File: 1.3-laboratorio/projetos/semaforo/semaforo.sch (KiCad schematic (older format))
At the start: 40 parts, among them U1 4093, U2 4093, U3 12V, U4 4017, U5 4017

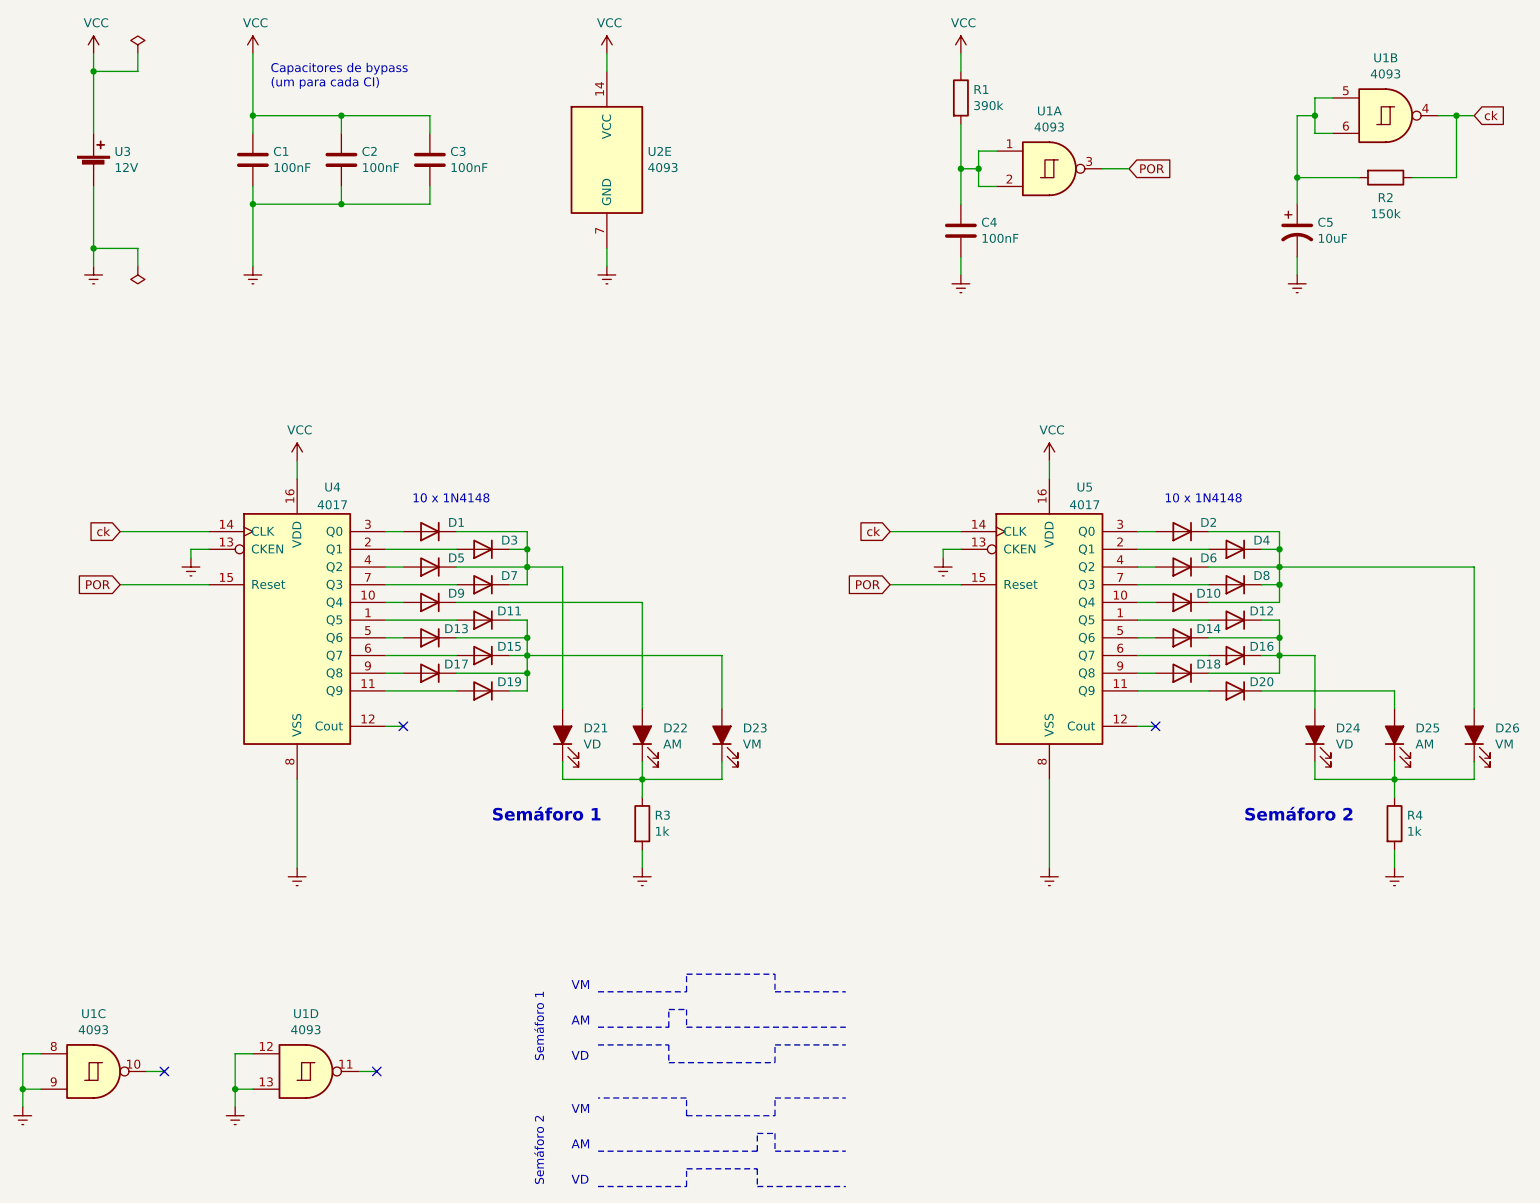
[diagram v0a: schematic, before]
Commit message: Projeto 'Deslocamento de LEDs Alternativo. Pequenas revisões nos outros dois projetos recém-criados. Fonte CC com novos padrões pré-definidos.
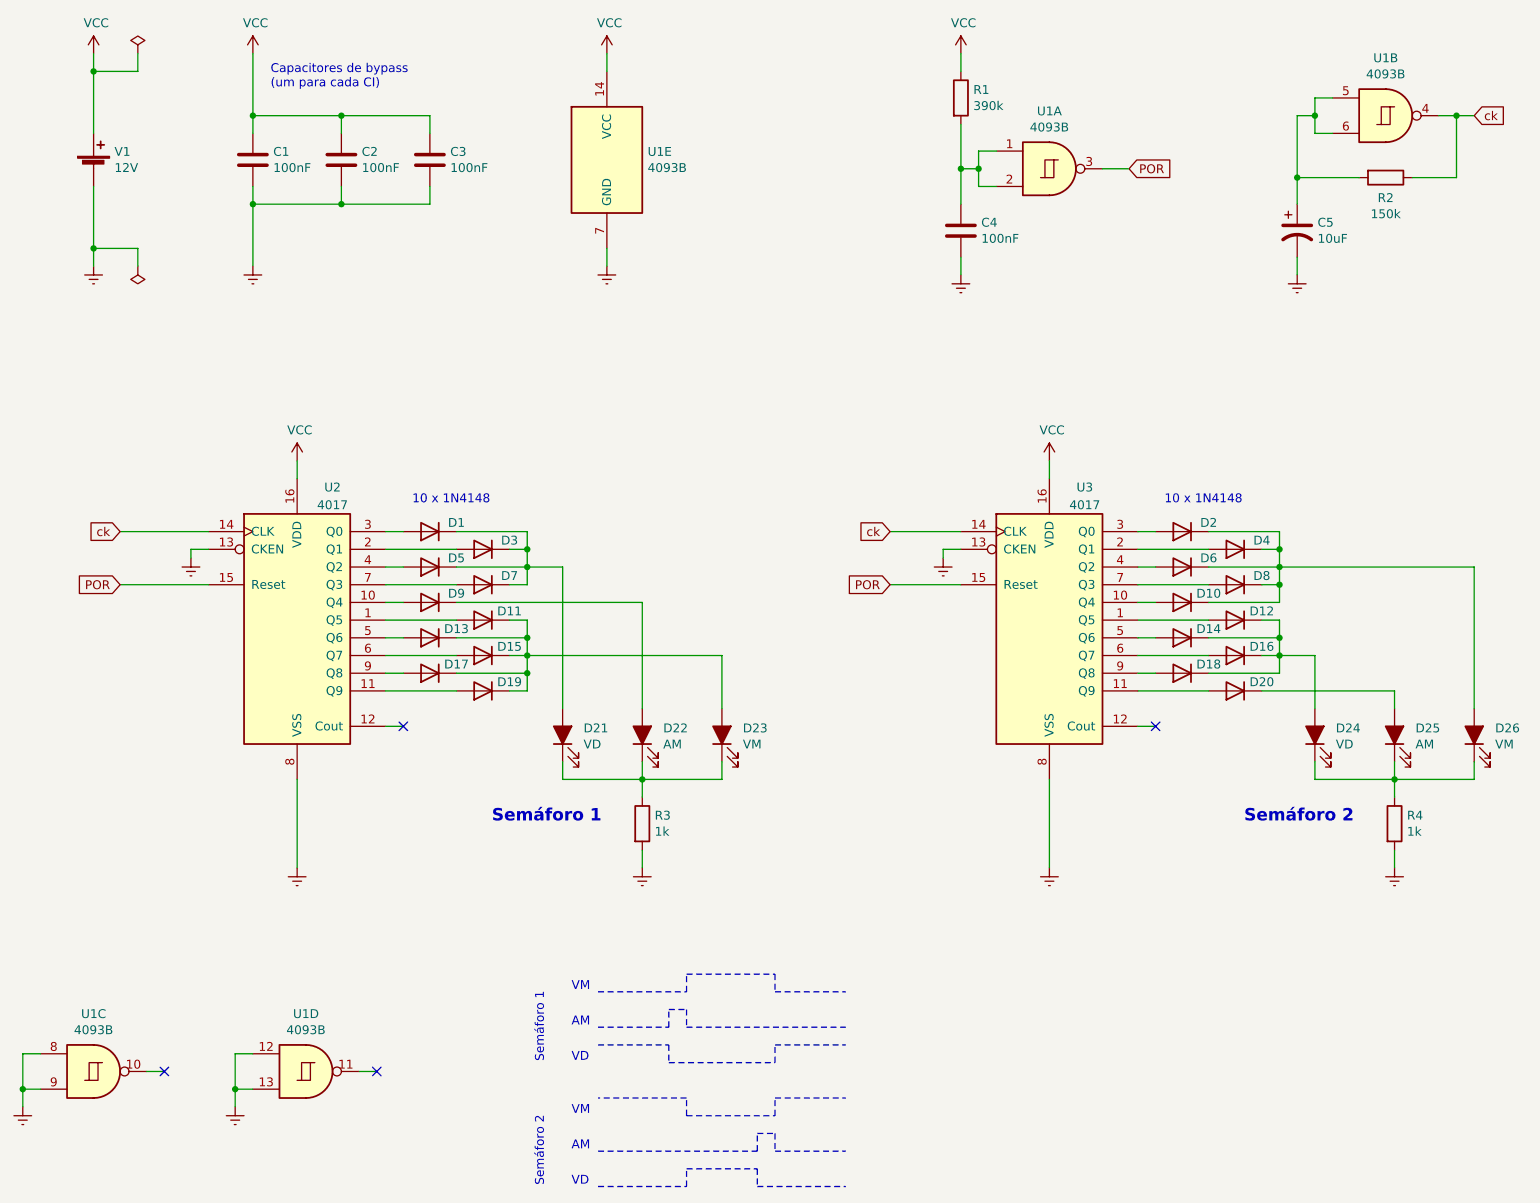
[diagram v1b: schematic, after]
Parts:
- U1: value 4093 -> 4093B; Value (none) -> 4093B
- U1: renamed from U2; value 4093 -> 4093B; Value (none) -> 4093B
- renumbered U4 to U2, U5 to U3, U3 to V1
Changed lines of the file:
@@
 $EndComp
 $Comp
-L 4xxx:4017 U4
+L 4xxx:4017 U2
 U 1 1 6163B9BC
 P 2950 4300
-F 0 "U4" H 3150 5050 50  0000 C CNN
+F 0 "U2" H 3150 5050 50  0000 C CNN
 F 1 "4017" H 3150 4950 50  0000 C CNN
 F 2 "" H 2950 4300 50  0001 C CNN
@@
 $EndComp
 $Comp
-L 4xxx:4017 U5
+L 4xxx:4017 U3
 U 1 1 6166B4F9
 P 7200 4300
-F 0 "U5" H 7400 5050 50  0000 C CNN
+F 0 "U3" H 7400 5050 50  0000 C CNN
 F 1 "4017" H 7400 4950 50  0000 C CNN
 F 2 "" H 7200 4300 50  0001 C CNN
@@
 	6600 3900 6600 3950
 $Comp
-L Device:Battery_Cell U3
+L Device:Battery_Cell V1
 U 1 1 61754F59
 P 1800 1750
-F 0 "U3" H 1918 1846 50  0000 L CNN
+F 0 "V1" H 1918 1846 50  0000 L CNN
 F 1 "12V" H 1918 1755 50  0000 L CNN
 F 2 "" V 1800 1810 50  0001 C CNN
@@
 P 9100 1450
 F 0 "U1" H 9100 1775 50  0000 C CNN
-F 1 "4093" H 9100 1684 50  0000 C CNN
+F 1 "4093B" H 9100 1684 50  0000 C CNN
 F 2 "" H 9100 1450 50  0001 C CNN
 F 3 "https://assets.nexperia.com/documents/data-sheet/HEF4093B.pdf" H 9100 1450 50  0001 C CNN
+F 4 "4093B" H 9100 1450 50  0001 C CNN "Value"
 	2    9100 1450
 	1    0    0    -1
@@
 P 7200 1750
 F 0 "U1" H 7200 2075 50  0000 C CNN
-F 1 "4093" H 7200 1984 50  0000 C CNN
+F 1 "4093B" H 7200 1984 50  0000 C CNN
 F 2 "" H 7200 1750 50  0001 C CNN
 F 3 "https://assets.nexperia.com/documents/data-sheet/HEF4093B.pdf" H 7200 1750 50  0001 C CNN
+F 4 "4093B" H 7200 1750 50  0001 C CNN "Value"
 	1    7200 1750
 	1    0    0    -1
 $EndComp
 $Comp
-L 4xxx:HEF4093B U2
+L 4xxx:HEF4093B U1
 U 5 1 617DCF2E
 P 4700 1700
-F 0 "U2" H 4930 1746 50  0000 L CNN
-F 1 "4093" H 4930 1655 50  0000 L CNN
+F 0 "U1" H 4930 1746 50  0000 L CNN
+F 1 "4093B" H 4930 1655 50  0000 L CNN
 F 2 "" H 4700 1700 50  0001 C CNN
 F 3 "https://assets.nexperia.com/documents/data-sheet/HEF4093B.pdf" H 4700 1700 50  0001 C CNN
+F 4 "4093B" H 4700 1700 50  0001 C CNN "Value"
 	5    4700 1700
 	1    0    0    -1
@@
 P 1800 6850
 F 0 "U1" H 1800 7175 50  0000 C CNN
-F 1 "4093" H 1800 7084 50  0000 C CNN
+F 1 "4093B" H 1800 7084 50  0000 C CNN
 F 2 "" H 1800 6850 50  0001 C CNN
 F 3 "https://assets.nexperia.com/documents/data-sheet/HEF4093B.pdf" H 1800 6850 50  0001 C CNN
+F 4 "4093B" H 1800 6850 50  0001 C CNN "Value"
 	3    1800 6850
 	1    0    0    -1
 $EndComp
 $Comp
-L power:Earth #PWR019
+L power:Earth #PWR018
 U 1 1 61858E3A
 P 1400 7050
-F 0 "#PWR019" H 1400 6800 50  0001 C CNN
+F 0 "#PWR018" H 1400 6800 50  0001 C CNN
 F 1 "Earth" H 1400 6900 50  0001 C CNN
 F 2 "" H 1400 7050 50  0001 C CNN
@@
 P 3000 6850
 F 0 "U1" H 3000 7175 50  0000 C CNN
-F 1 "4093" H 3000 7084 50  0000 C CNN
+F 1 "4093B" H 3000 7084 50  0000 C CNN
 F 2 "" H 3000 6850 50  0001 C CNN
 F 3 "https://assets.nexperia.com/documents/data-sheet/HEF4093B.pdf" H 3000 6850 50  0001 C CNN
+F 4 "4093B" H 3000 6850 50  0001 C CNN "Value"
 	4    3000 6850
 	1    0    0    -1
 $EndComp
 $Comp
-L power:Earth #PWR018
+L power:Earth #PWR019
 U 1 1 61876FE1
 P 2600 7050
-F 0 "#PWR018" H 2600 6800 50  0001 C CNN
+F 0 "#PWR019" H 2600 6800 50  0001 C CNN
 F 1 "Earth" H 2600 6900 50  0001 C CNN
 F 2 "" H 2600 7050 50  0001 C CNN
@@
 Semáforo 2
 $Comp
-L power:PWR_FLAG #FLG?
+L power:PWR_FLAG #FLG01
 U 1 1 619906C4
 P 2050 1100
-F 0 "#FLG?" H 2050 1175 50  0001 C CNN
+F 0 "#FLG01" H 2050 1175 50  0001 C CNN
 F 1 "PWR_FLAG" H 2050 1273 50  0001 C CNN
 F 2 "" H 2050 1100 50  0001 C CNN
@@
 	1800 1200 1800 1550
 $Comp
-L power:PWR_FLAG #FLG?
+L power:PWR_FLAG #FLG02
 U 1 1 61997AEB
 P 2050 2300
-F 0 "#FLG?" H 2050 2375 50  0001 C CNN
+F 0 "#FLG02" H 2050 2375 50  0001 C CNN
 F 1 "PWR_FLAG" H 2050 2473 50  0001 C CNN
 F 2 "" H 2050 2300 50  0001 C CNN
